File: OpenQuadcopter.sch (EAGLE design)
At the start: 36 parts, among them U1 MPU-6000QFN-24

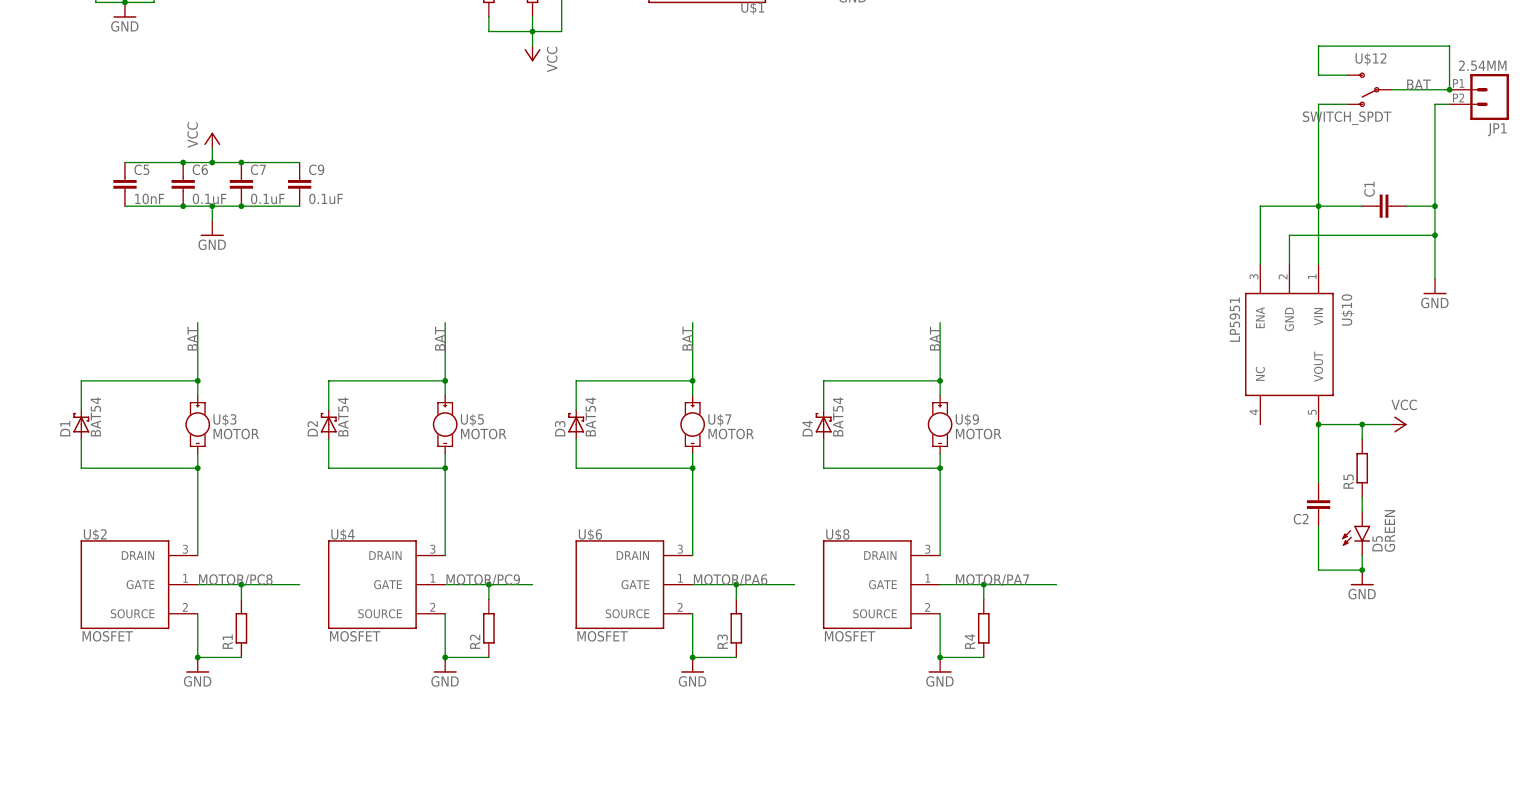
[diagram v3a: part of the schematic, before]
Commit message: update lbr/openmotestm.lbr
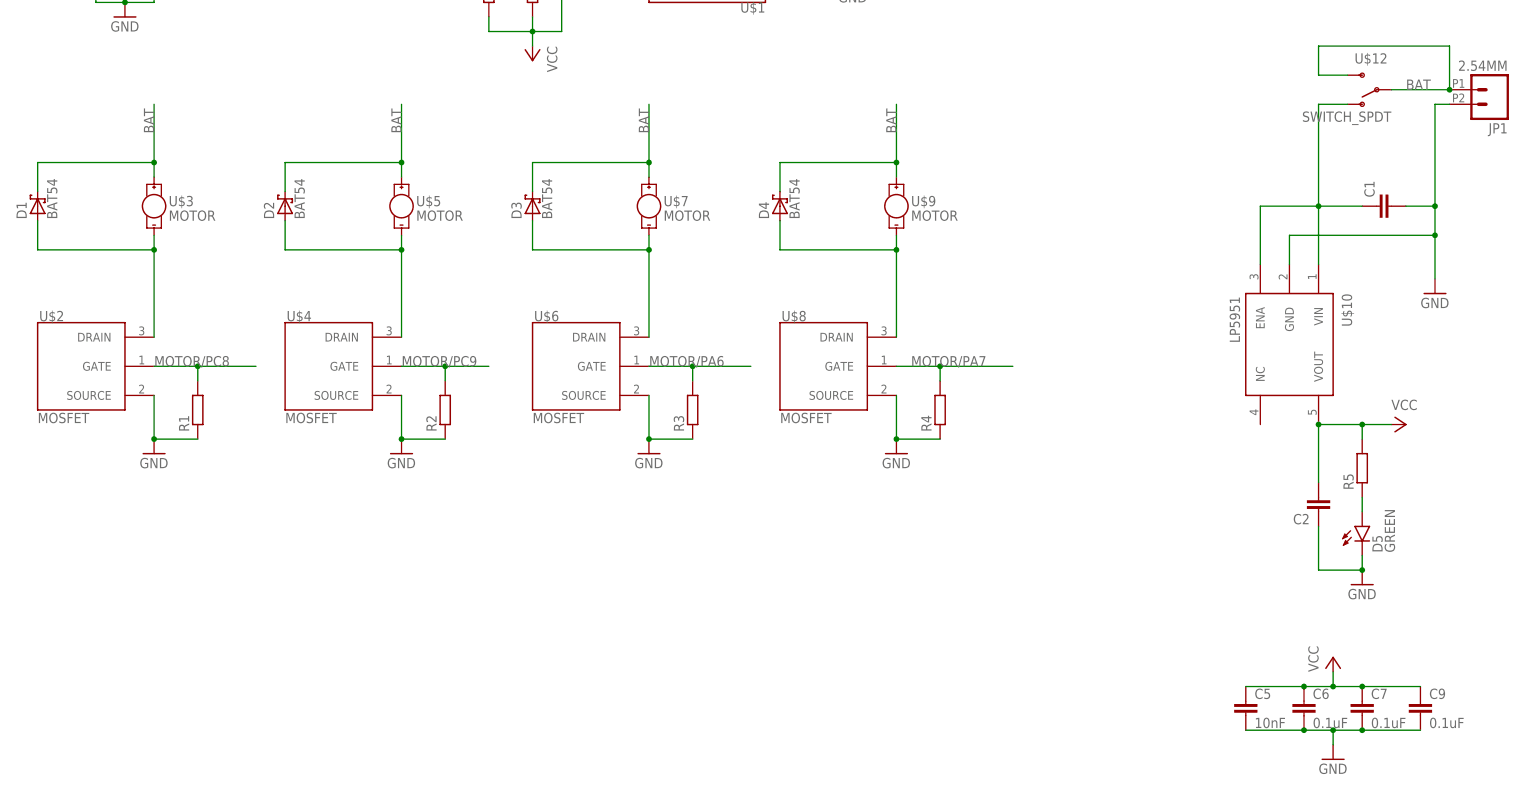
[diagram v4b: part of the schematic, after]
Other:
- moved on the sheet: C5, C6, C7, C9, D1, D2, D3, D4, R1, R2, R3, R4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

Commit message: update openmotestm
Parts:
- added C10, C13, C14, C15, C16, C17, C18, C19, C20, C21, C22, C23, C8: (no value), openmotestm:C-EUC0402
- added C24: (no value), openmotestm:C-EUC0603
- added D6, D7: GREEN, openmotestm:LED-GREEN0603
- added JP2: USB_MICROB, openmotestm:USB_MICROB_PLUGCONN-11752
- added R10, R11, R12, R13, R14, R15, R16, R17, R18, R19, R20, R21, R22, R23, R24, R25, R26, R27, R28, R8, R9: (no value), openmotestm:R-EU_R0402
- added U$13: BQ24075, openmotestm:BQ24075
- added U$14: CP2102, openmotestm:CP2102
- added U$15, U$16: TPS79301, openmotestm:TPS79301
- added U$17, U$20: 2N7002, openmotestm:2N7002
- added U$18: MAX16054, openmotestm:MAX16054
- added U$19: BUTTON, openmotestm:BUTTON
- added U$21, U$22: 1X2, openmotestm:1X2
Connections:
- new net /CHG: U$13./CHG
- new net /PGOOD: R17.2, R18.1, U$13./PGOOD
- new net AGND: C16.2, C17.2, R14.1, R27.2
- new net DGND: C19.2, C21.1, C23.2, C24.2, D6.C, D7.C, JP2.GND, R16.1, R28.2, U$14.GND29, U$22.2
- new net EN1: U$13.EN1
- new net EN2: U$13.EN2
- new net N$15: R21.1, U$18./OUT
- new net N$18: R8.2, U$13.ILIM
- new net N$19: R9.2, U$13.TMR
- new net N$20: R10.2, U$13.ISET
- new net N$21: R11.2, U$13.TS
- new net N$23: R21.2, U$13.SYSOFF, U$17.D
- new net N$24: C14.1, R12.2, U$15.EN, U$15.IN
- new net N$25: U$18.IN, U$19.2
- new net N$26: C15.2, R13.1, R14.2, U$15.FB
- new net N$27: C17.1, U$15.NR
- new net N$28: C19.1, U$16.NR
- new net N$29: C20.2, R15.1, R16.2, R17.1, U$16.FB
- new net N$30: C22.1, R24.2, U$20.S
- new net N$32: D6.A, R19.1
- new net N$33: D7.A, R20.1
- new net N$34: R26.1, U$20.D
- new net N$35: JP2.D+, U$14.D+
- new net N$36: JP2.D-, U$14.D-
- new net SYSOFF: R23.2, U$18.CLR
- new net V+: C10.1, C13.1, C18.1, C8.1, R12.1, U$13.BAT2, U$13.BAT3, U$13.OUT10, U$13.OUT11, U$16.EN, U$16.IN
- new net VBUS: C23.1, C24.1, JP2.VCC, R22.2, U$13.IN, U$14.REGIN, U$14.VBUS, U$17.G, U$22.1
- new net VCCA: R6.2, R7.2, U$1.S1, U$1.VDD, U$1.VDDIO, U1.AD0/SDO, U1.CS, U1.VDD
- new net VCCD: U$11.VDD
- new net VCOM: R25.2, U$20.G
- net BAT: now also R26.2, U$18.VCC, U$21.1
- net GND: now also C10.2, C13.2, C14.2, C18.2, C22.2, C8.2, R10.1, R11.1, R22.1, R23.1, R24.1, R25.1, R27.1, R28.1, R8.1, R9.1, U$13./CE, U$13.TPAD, U$13.VSS, U$15.GND, U$16.GND, U$17.S, U$18.GND, U$21.2
- net PA10: now also U$14.TXD
- net PA11: now also U$14.CTS
- net PA12: now also U$14.RTS
- net PA9: now also U$14.RXD
- net VCC: now also C15.1, C16.1, C20.1, C21.2, R13.2, R15.2, R18.2, R19.2, R20.2, U$15.OUT, U$16.OUT; no longer R6.2, R7.2, U$1.S1, U$1.VDD, U$1.VDDIO, U$11.VDD, U1.AD0/SDO, U1.CS, U1.VDD

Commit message: drawing quadcopter
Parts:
- removed C1, C2: (no value), rcl:C-EUC0603
- removed D5: GREEN, openmotestm:LED-GREEN0603
- removed R5: (no value), rcl:R-EU_R0402
- removed U$10: LP5951, openmotestm:LP5951
- removed U$21: 1X2, openmotestm:1X2
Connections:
- removed net N$10: C1.1, U$10.ENA, U$10.VIN, U$12.O
- removed net N$17: D5.A, R5.1
- removed net V+: C10.1, C13.1, C18.1, C8.1, R12.1, U$13.BAT2, U$13.BAT3, U$13.OUT10, U$13.OUT11, U$16.EN, U$16.IN
- removed net VCC: C15.1, C16.1, C2.2, C20.1, C21.2, C5.1, C6.1, C7.1, C9.1, R13.2, R15.2, R18.2, R19.2, R20.2, R5.2, U$10.VOUT, U$15.OUT, U$16.OUT
- new net BATTERY_IN: JP1.1, U$12.P, U$12.S
- net BAT: now also C8.1, U$12.O, U$13.BAT2, U$13.BAT3; no longer JP1.1, U$12.P, U$12.S, U$21.1
- net GND: no longer C1.2, C2.1, D5.C, U$10.GND, U$21.2
- net VCCA: now also C15.1, C16.1, C5.1, C6.1, C7.1, C9.1, R13.2, U$15.OUT
- net VCCD: now also C20.1, C21.2, R15.2, R18.2, R19.2, R20.2, U$16.OUT
- net VCOM: now also C10.1, C13.1, C18.1, R12.1, U$13.OUT10, U$13.OUT11, U$16.EN, U$16.IN

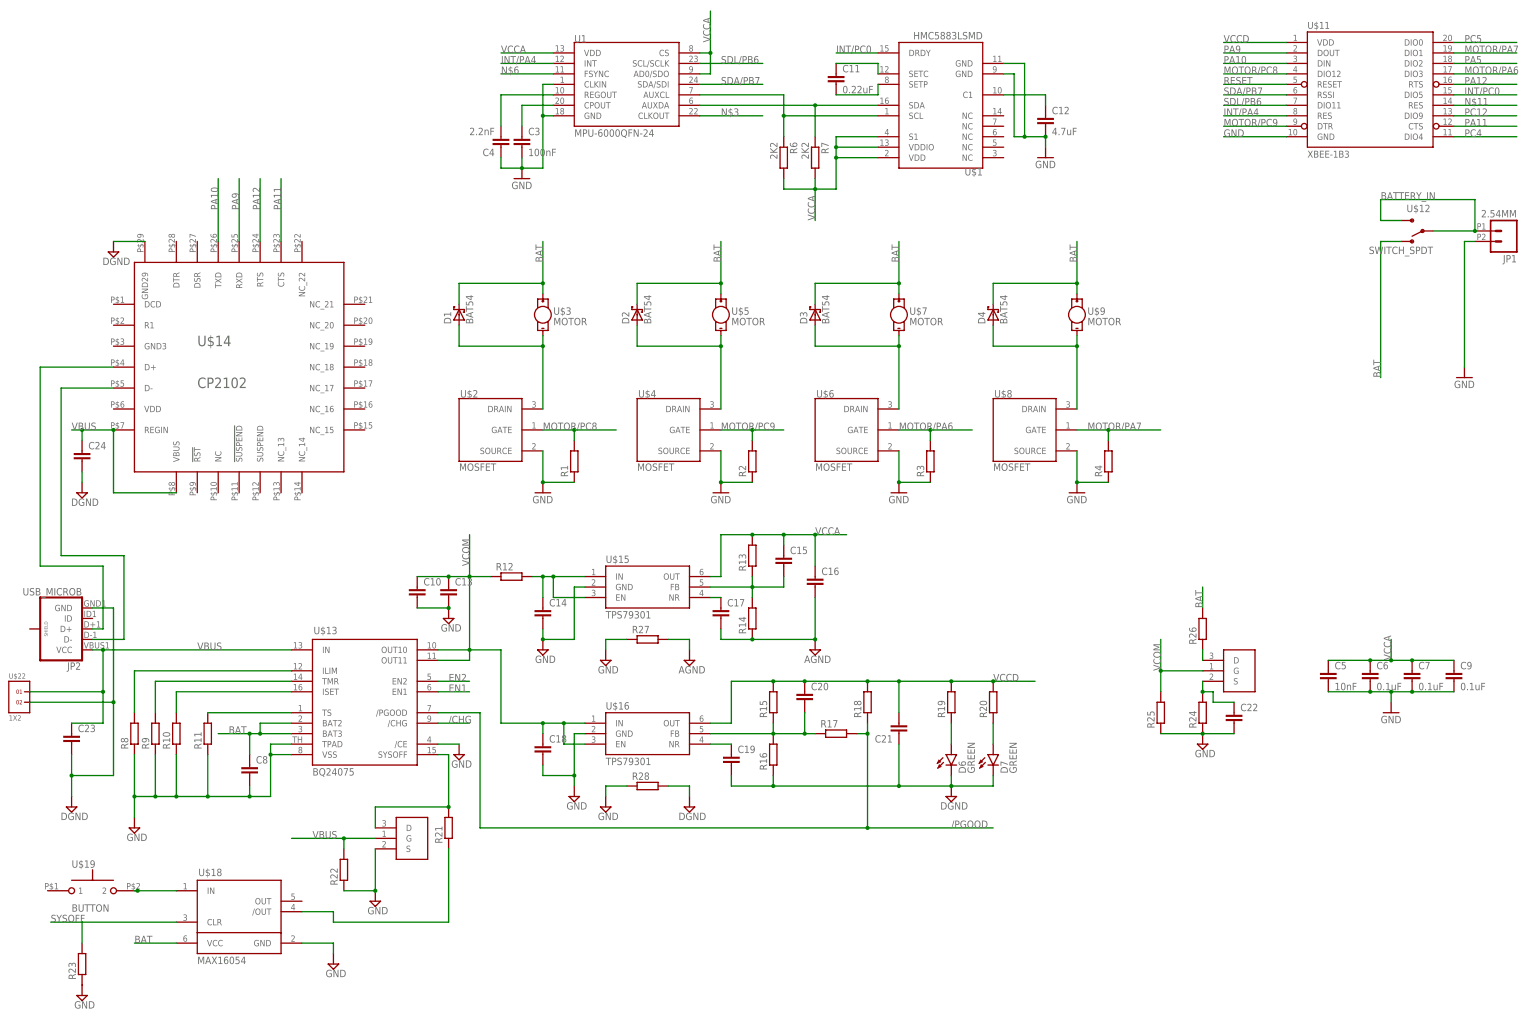
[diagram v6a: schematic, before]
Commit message: Add XBee-Explorer-Dongle-Sparkfun. Update openmotestm. arrange the layout of openquadcopter board.
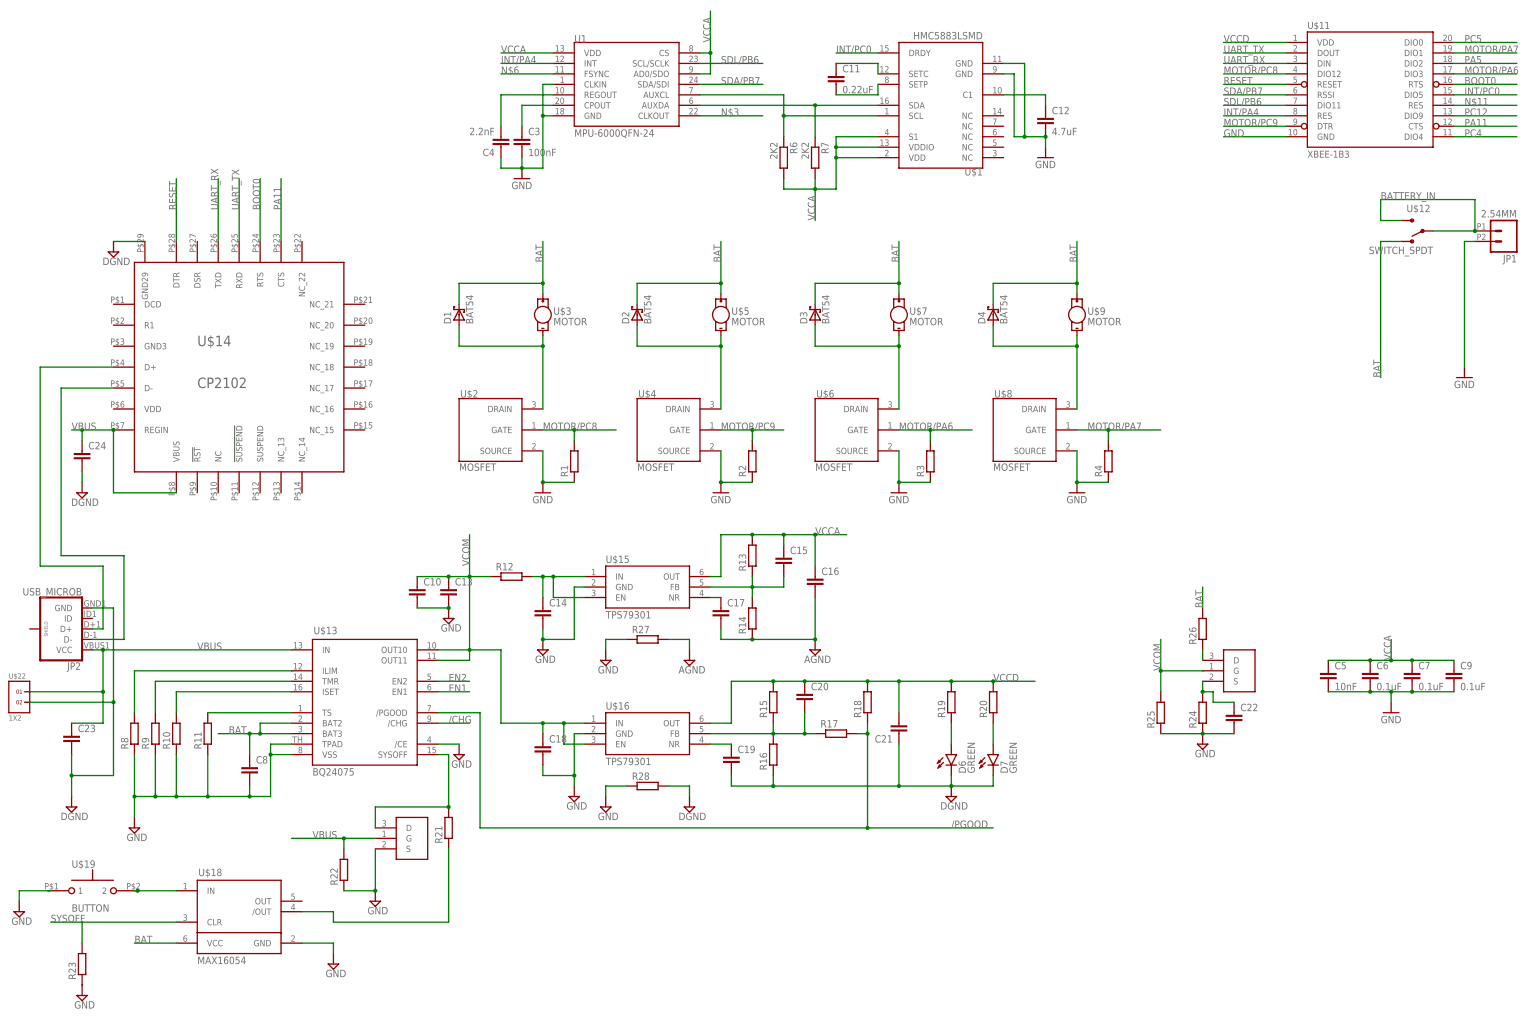
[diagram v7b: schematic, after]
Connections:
- net PA10 renamed UART_RX
- net PA12 renamed BOOT0
- net PA9 renamed UART_TX
- net RESET: now also U$14.DTR
